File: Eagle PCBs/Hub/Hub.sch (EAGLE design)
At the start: 10 parts

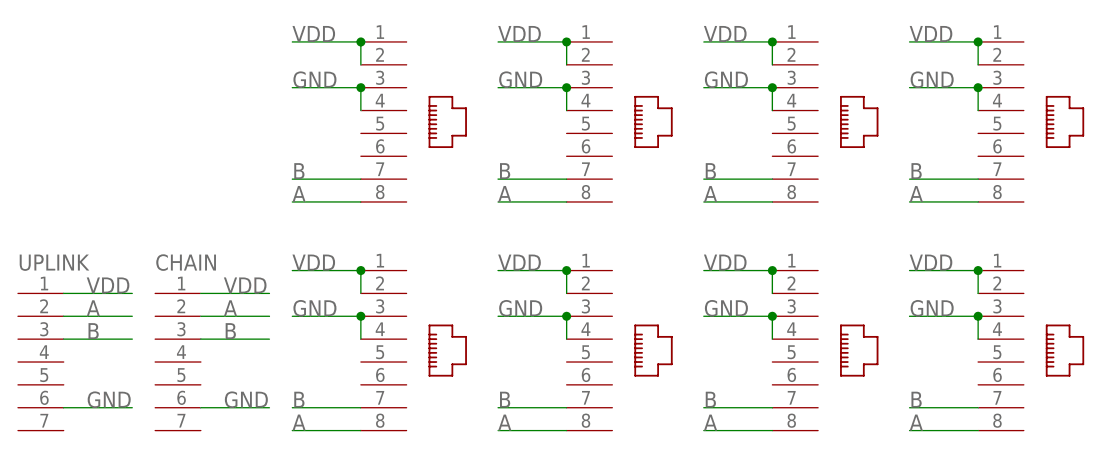
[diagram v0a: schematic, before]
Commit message: Added a 5v bus to all PCBs
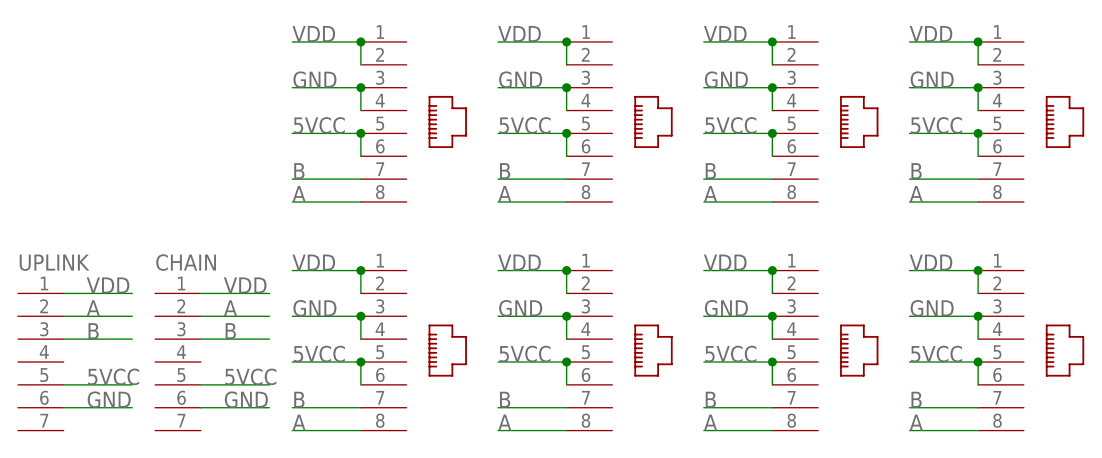
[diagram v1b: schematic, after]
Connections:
- new net 5VCC: 1.5, 1.6, 2.5, 2.6, 3.5, 3.6, 4.5, 4.6, 5.5, 5.6, 6.5, 6.6, 7.5, 7.6, 8.5, 8.6, CHAIN.5, UPLINK.5
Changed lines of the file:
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@@
 <clearance class="0" value="0.1524"/>
+</class>
+<class number="1" name="5VCC" width="0.8382" drill="0.5334">
+<clearance class="1" value="0.1524"/>
 </class>
 </classes>
@@
 </segment>
 </net>
+<net name="5VCC" class="1">
+<segment>
+<pinref part="UPLINK" gate="G$1" pin="5"/>
+<wire x1="7.62" y1="7.62" x2="15.24" y2="7.62" width="0.1524" layer="91"/>
+<label x="10.16" y="7.62" size="1.778" layer="95"/>
+</segment>
+<segment>
+<wire x1="22.86" y1="7.62" x2="30.48" y2="7.62" width="0.1524" layer="91"/>
+<label x="25.4" y="7.62" size="1.778" layer="95"/>
+<pinref part="CHAIN" gate="G$1" pin="5"/>
+</segment>
+<segment>
+<wire x1="33.02" y1="35.56" x2="40.64" y2="35.56" width="0.1524" layer="91"/>
+<label x="33.02" y="35.56" size="1.778" layer="95"/>
+<wire x1="40.64" y1="35.56" x2="40.64" y2="33.02" width="0.1524" layer="91"/>
+<pinref part="1" gate="G$1" pin="5"/>
+<junction x="40.64" y="35.56"/>
+<pinref part="1" gate="G$1" pin="6"/>
+</segment>
+<segment>
+<wire x1="55.88" y1="35.56" x2="63.5" y2="35.56" width="0.1524" layer="91"/>
+<label x="55.88" y="35.56" size="1.778" layer="95"/>
+<pinref part="2" gate="G$1" pin="5"/>
+<pinref part="2" gate="G$1" pin="6"/>
+<wire x1="63.5" y1="33.02" x2="63.5" y2="35.56" width="0.1524" layer="91"/>
+<junction x="63.5" y="35.56"/>
+</segment>
+<segment>
+<wire x1="78.74" y1="35.56" x2="86.36" y2="35.56" width="0.1524" layer="91"/>
+<label x="78.74" y="35.56" size="1.778" layer="95"/>
+<pinref part="3" gate="G$1" pin="5"/>
+<pinref part="3" gate="G$1" pin="6"/>
+<wire x1="86.36" y1="33.02" x2="86.36" y2="35.56" width="0.1524" layer="91"/>
+<junction x="86.36" y="35.56"/>
+</segment>
+<segment>
+<wire x1="101.6" y1="35.56" x2="109.22" y2="35.56" width="0.1524" layer="91"/>
+<label x="101.6" y="35.56" size="1.778" layer="95"/>
+<pinref part="4" gate="G$1" pin="5"/>
+<pinref part="4" gate="G$1" pin="6"/>
+<wire x1="109.22" y1="33.02" x2="109.22" y2="35.56" width="0.1524" layer="91"/>
+<junction x="109.22" y="35.56"/>
+</segment>
+<segment>
+<wire x1="55.88" y1="10.16" x2="63.5" y2="10.16" width="0.1524" layer="91"/>
+<label x="55.88" y="10.16" size="1.778" layer="95"/>
+<pinref part="6" gate="G$1" pin="5"/>
+<pinref part="6" gate="G$1" pin="6"/>
+<wire x1="63.5" y1="7.62" x2="63.5" y2="10.16" width="0.1524" layer="91"/>
+<junction x="63.5" y="10.16"/>
+</segment>
+<segment>
+<wire x1="33.02" y1="10.16" x2="40.64" y2="10.16" width="0.1524" layer="91"/>
+<label x="33.02" y="10.16" size="1.778" layer="95"/>
+<pinref part="5" gate="G$1" pin="5"/>
+<pinref part="5" gate="G$1" pin="6"/>
+<wire x1="40.64" y1="7.62" x2="40.64" y2="10.16" width="0.1524" layer="91"/>
+<junction x="40.64" y="10.16"/>
+</segment>
+<segment>
+<wire x1="78.74" y1="10.16" x2="86.36" y2="10.16" width="0.1524" layer="91"/>
+<label x="78.74" y="10.16" size="1.778" layer="95"/>
+<pinref part="7" gate="G$1" pin="5"/>
+<pinref part="7" gate="G$1" pin="6"/>
+<wire x1="86.36" y1="7.62" x2="86.36" y2="10.16" width="0.1524" layer="91"/>
+<junction x="86.36" y="10.16"/>
+</segment>
+<segment>
+<wire x1="101.6" y1="10.16" x2="109.22" y2="10.16" width="0.1524" layer="91"/>
+<label x="101.6" y="10.16" size="1.778" layer="95"/>
+<pinref part="8" gate="G$1" pin="5"/>
+<pinref part="8" gate="G$1" pin="6"/>
+<wire x1="109.22" y1="7.62" x2="109.22" y2="10.16" width="0.1524" layer="91"/>
+<junction x="109.22" y="10.16"/>
+</segment>
+</net>
